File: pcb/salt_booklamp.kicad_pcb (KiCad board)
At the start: 2 copper layers, 45.1 x 45.1 mm, 24 parts, among them J1 USB-C31-S-RA-CS1E-BK-T/R, P1 PIC-TC2050-IDC, U1 PIC16F15213-I/SN, U2 BQ21040DBVR, U3 TPS61158DRVR

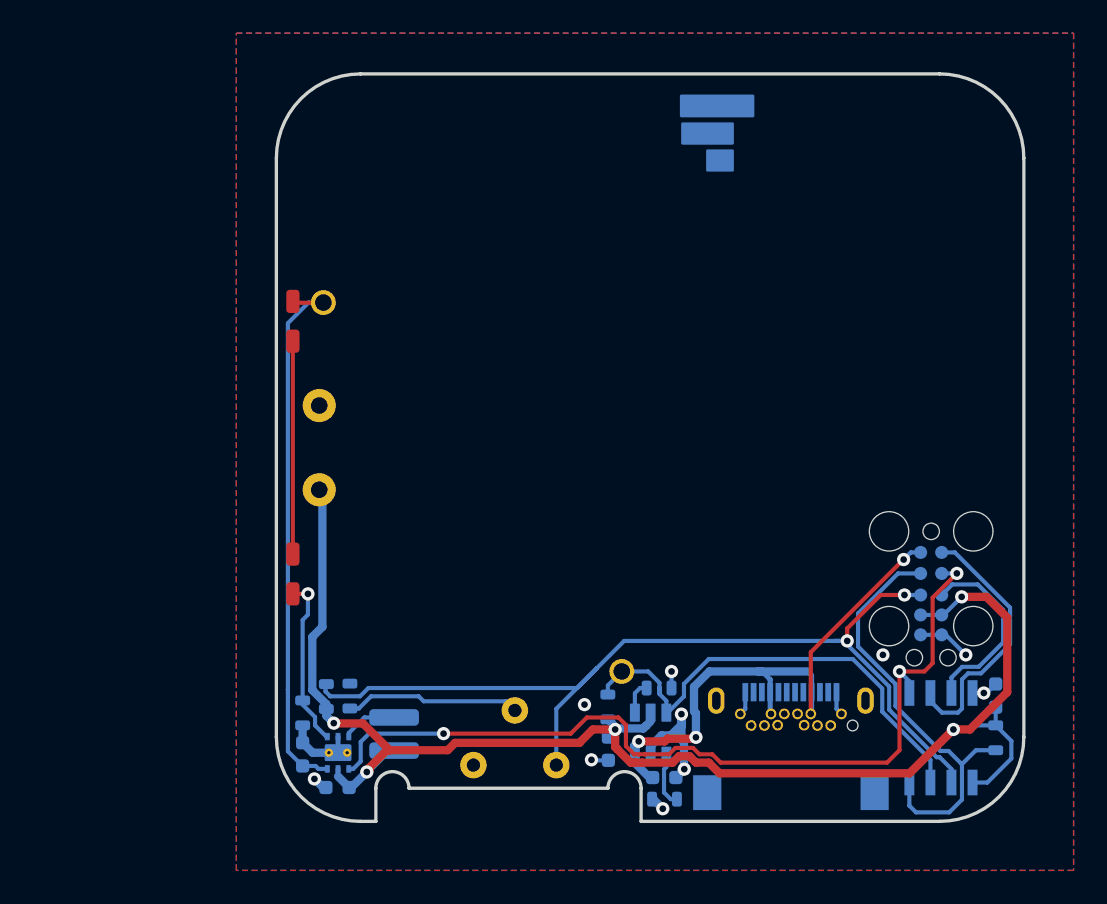
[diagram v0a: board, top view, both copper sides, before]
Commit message: Changed 0603 parts to 0402, assigned 0402 uF cap MPN, still need to assign 0402 Resistor MPNs
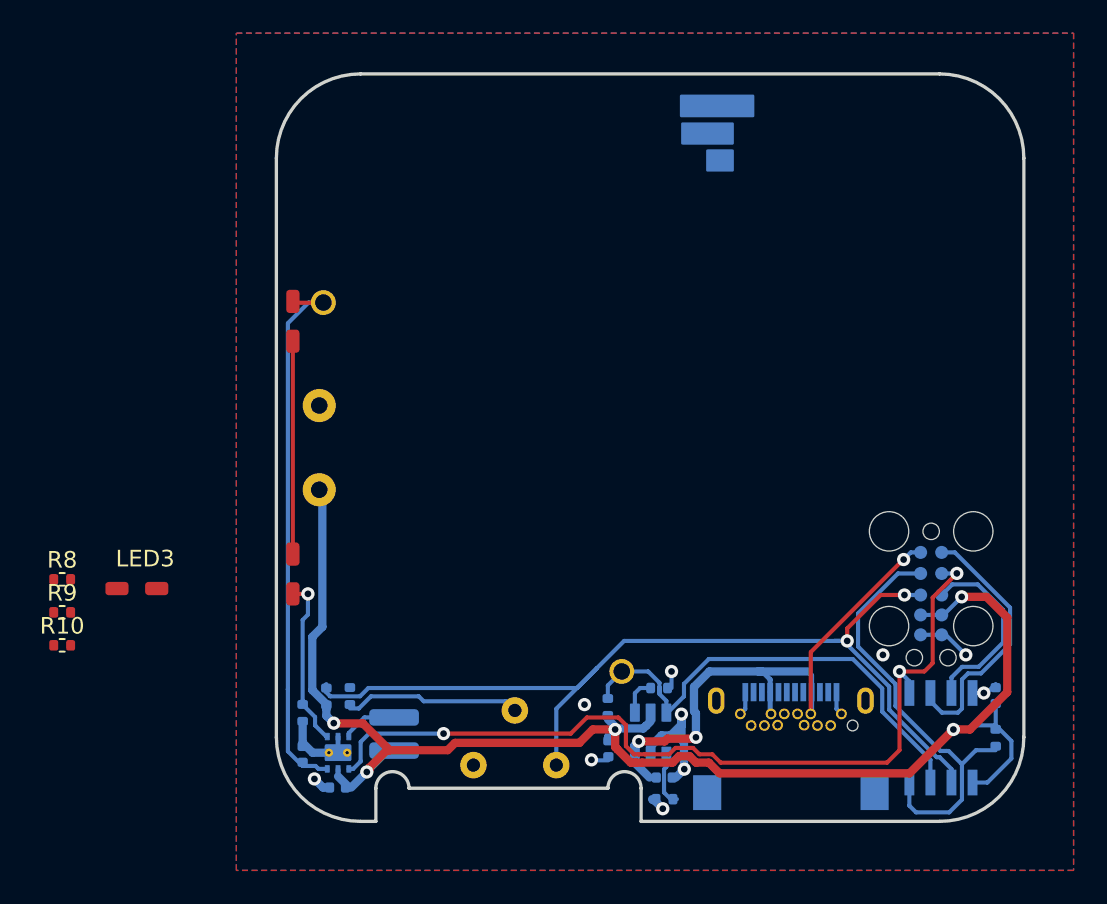
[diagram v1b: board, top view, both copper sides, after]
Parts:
- added LED3: SMS1105UWDW, salt_booklamp_footprints:LED_SMS1105UWDW, F.Cu at (193.3, 137.5)
- added R10: 5k1, Resistor_SMD:R_0402_1005Metric, F.Cu at (188.8, 141.0)
- added R8: 0r0, Resistor_SMD:R_0402_1005Metric, F.Cu at (188.8, 137.0)
- added R9: 5k1, Resistor_SMD:R_0402_1005Metric, F.Cu at (188.8, 139.0)
- C1, C2, C3, C4, C5: footprint salt_booklamp_footprints:cap_0603 -> Capacitor_SMD:C_0402_1005Metric
- R1, R2, R3, R4, R5, R6, R7: footprint salt_booklamp_footprints:res_0603 -> Resistor_SMD:R_0402_1005Metric
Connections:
- J1 pad A5: unconnected-(J1-CC1-PadA5) -> Net-(J1-CC1)
- J1 pad B5: unconnected-(J1-CC2-PadB5) -> Net-(J1-CC2)
- LED2 pad A: Net-(LED1-k) -> Net-(LED2-a)

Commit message: Changed MCU to smaller DFN package, add Connector footprint to PCB (very big), add shield pins to USB footprint to remove warning
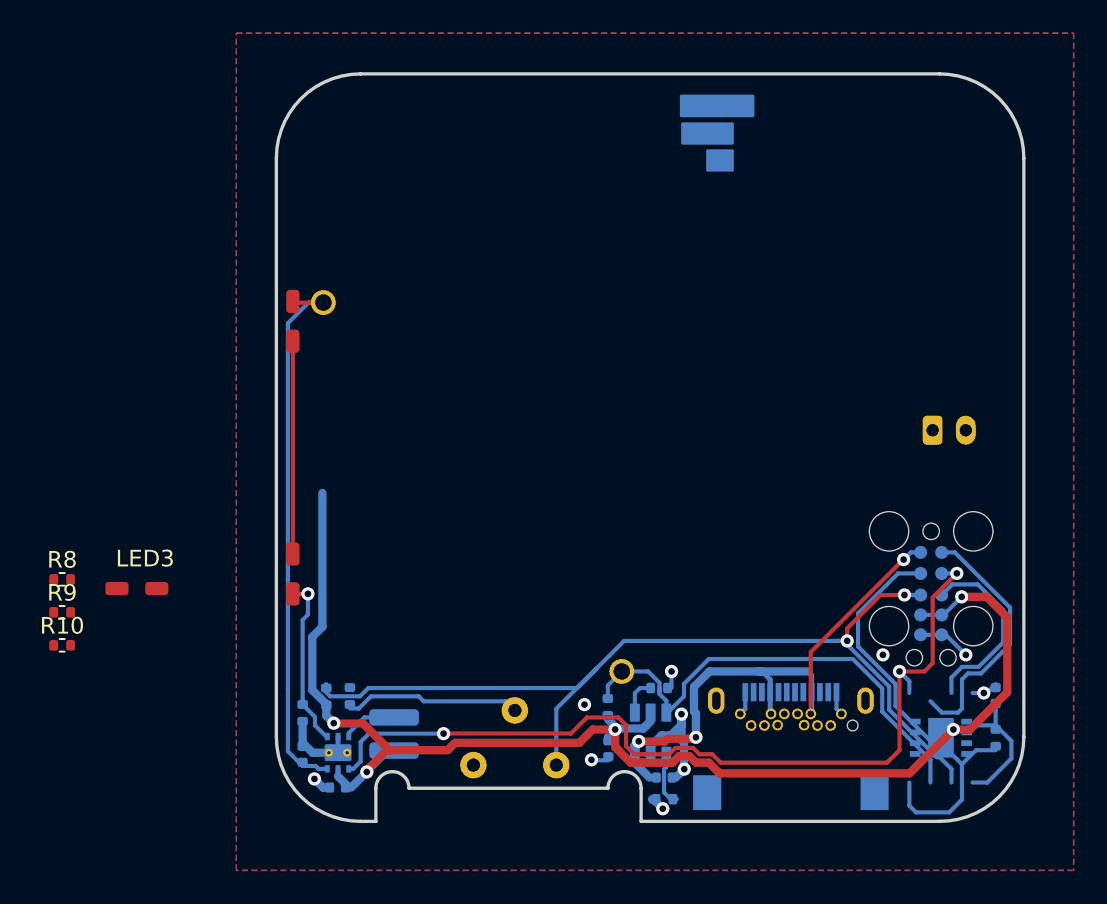
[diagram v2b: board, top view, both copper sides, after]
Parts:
- BATT1: value 1578 -> S2B-PH-K-S; footprint salt_booklamp_footprints:PRT-13851 -> GymTimer:JST_PH_S2B-PH-K_1x02_P2.00mm_Horizontal
- U1: footprint salt_booklamp_footprints:SOIC-8 - PIC16F15213 -> GymTimer:DFN-8-1EP_3x3mm_P0.65mm_EP1.55x2.4mm
- moved BATT1 37.0 mm to (241.3, 128.0), turned to 0 degrees
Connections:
- BATT1 pad 1: +3.7_VBATT -> GND
- BATT1 pad 2: GND -> +3.7_VBATT
- J1 pad 0: (no net) -> GND

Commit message: Start placement - new LED placement
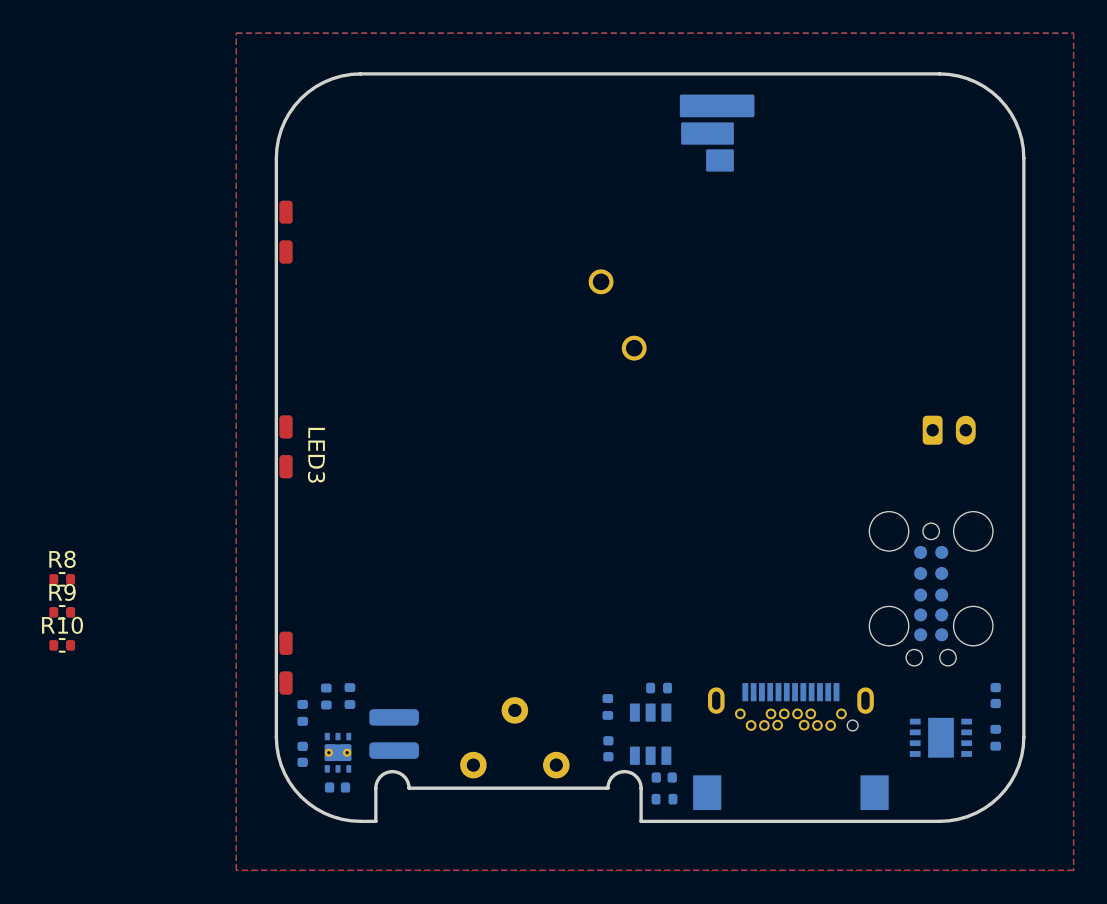
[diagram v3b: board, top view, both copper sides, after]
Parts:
- moved ~{TP_CHG}1 19.5 mm to (223.3, 123.0)
- moved TP_LED_DRV1 16.8 mm to (221.3, 119.0)
- moved LED3 12.4 mm to (202.3, 129.0), turned to -90 degrees
- moved LED2 5.40 mm to (202.3, 142.0)
- moved LED1 5.40 mm to (202.3, 116.0)
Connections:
- R5 pad 1: Net-(P1-~{MCLR}) -> Net-(P1-ICSPDAT)
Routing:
- net +3.7_VBATT: track 91.4 -> 0.00 mm, vias 5 -> 0
- net /~{SWITCH}: track 58.2 -> 0.00 mm, vias 2 -> 0
- net /LED_CTRL: track 53.1 -> 0.00 mm, vias 3 -> 0
- net +5V_USB: track 34.9 -> 0.00 mm, vias 3 -> 0
- net /LED_DRV: track 33.1 -> 0.00 mm
- net /~{CHARGING}: track 29.2 -> 0.00 mm
- net Net-(P1-~{MCLR}): track 26.3 -> 0.00 mm
- net GND: track 22.8 -> 0.00 mm, vias 10 -> 0
- net Net-(P1-ICSPCLK): track 15.5 -> 0.00 mm
- net Net-(LED1-k): track 12.8 -> 0.00 mm
- net Net-(P1-ICSPDAT): track 11.5 -> 0.00 mm
- net Net-(R7-Pad2): track 10.6 -> 0.00 mm
- net Net-(LED2-k): track 10.3 -> 0.00 mm, vias 1 -> 0
- net Net-(U3-LX): track 3.33 -> 0.00 mm
- net Net-(U2-ISET): track 3.22 -> 0.00 mm
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
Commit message: Placement work
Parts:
- R10, R8, R9: moved to B.Cu
- moved R10 10.5 mm to (196.0, 148.5), turned to 180 degrees
- moved R8 10.5 mm to (196.0, 144.6), turned to 180 degrees
- moved R9 10.5 mm to (196.0, 146.5), turned to 180 degrees
- moved R7 2.05 mm to (205.8, 146.0)
- moved R3 1.99 mm to (204.7, 146.0)
- moved R2 1.77 mm to (203.5, 146.8)
- moved C4 1.27 mm to (203.5, 148.8)
- moved U3 0.99 mm to (205.4, 148.4)
- moved C5 0.75 mm to (205.4, 150.3)

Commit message: Placement work
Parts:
- moved R8 2.79 mm to (198.8, 145.0)
- moved R10 2.79 mm to (198.8, 149.0)
- moved R9 2.79 mm to (198.8, 147.0)
- moved R4 0.37 mm to (221.8, 145.0)
- moved R6 0.22 mm to (225.0, 150.0)
- moved C1 0.06 mm to (225.0, 148.9)
- moved C2 0.06 mm to (221.8, 147.2)
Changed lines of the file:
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@@
 			(psa4output no)
 			(plot_black_and_white yes)
-			(plotinvisibletext no)
 			(sketchpadsonfab no)
 			(plotpadnumbers no)
@@
 	(footprint "Capacitor_SMD:C_0402_1005Metric"
 		(layer "B.Cu")
-		(at 225.093116 148.932371)
+		(at 225.032 148.932371)
 		(descr "Capacitor SMD 0402 (1005 Metric), square (rectangular) end terminal, IPC_7351 nominal, (Body size source: IPC-SM-782 page 76, https://www.pcb-3d.com/wordpress/wp-content/uploads/ipc-sm-782a_amendment_1_and_2.pdf), generated with kicad-footprint-generator")
 		(tags "capacitor")
@@
 	(footprint "Resistor_SMD:R_0402_1005Metric"
 		(layer "B.Cu")
-		(at 196.032 148.532 180)
+		(at 198.782 149.012 180)
 		(descr "Resistor SMD 0402 (1005 Metric), square (rectangular) end terminal, IPC_7351 nominal, (Body size source: IPC-SM-782 page 72, https://www.pcb-3d.com/wordpress/wp-content/uploads/ipc-sm-782a_amendment_1_and_2.pdf), generated with kicad-footprint-generator")
 		(tags "resistor")
@@
 	(footprint "Capacitor_SMD:C_0402_1005Metric"
 		(layer "B.Cu")
-		(at 221.721579 147.194047 -90)
+		(at 221.782 147.194047 -90)
 		(descr "Capacitor SMD 0402 (1005 Metric), square (rectangular) end terminal, IPC_7351 nominal, (Body size source: IPC-SM-782 page 76, https://www.pcb-3d.com/wordpress/wp-content/uploads/ipc-sm-782a_amendment_1_and_2.pdf), generated with kicad-footprint-generator")
 		(tags "capacitor")
@@
 	(footprint "Resistor_SMD:R_0402_1005Metric"
 		(layer "B.Cu")
-		(at 225.107866 150.236383 180)
+		(at 225.032 150.032 180)
 		(descr "Resistor SMD 0402 (1005 Metric), square (rectangular) end terminal, IPC_7351 nominal, (Body size source: IPC-SM-782 page 72, https://www.pcb-3d.com/wordpress/wp-content/uploads/ipc-sm-782a_amendment_1_and_2.pdf), generated with kicad-footprint-generator")
 		(tags "resistor")
@@
 	(footprint "Resistor_SMD:R_0402_1005Metric"
 		(layer "B.Cu")
-		(at 196.032 146.542 180)
+		(at 198.782 147.022 180)
 		(descr "Resistor SMD 0402 (1005 Metric), square (rectangular) end terminal, IPC_7351 nominal, (Body size source: IPC-SM-782 page 72, https://www.pcb-3d.com/wordpress/wp-content/uploads/ipc-sm-782a_amendment_1_and_2.pdf), generated with kicad-footprint-generator")
 		(tags "resistor")
@@
 	(footprint "Resistor_SMD:R_0402_1005Metric"
 		(layer "B.Cu")
-		(at 221.689761 144.674153 -90)
+		(at 221.782 145.032 -90)
 		(descr "Resistor SMD 0402 (1005 Metric), square (rectangular) end terminal, IPC_7351 nominal, (Body size source: IPC-SM-782 page 72, https://www.pcb-3d.com/wordpress/wp-content/uploads/ipc-sm-782a_amendment_1_and_2.pdf), generated with kicad-footprint-generator")
 		(tags "resistor")
@@
 	(footprint "Resistor_SMD:R_0402_1005Metric"
 		(layer "B.Cu")
-		(at 196.032 144.552 180)
+		(at 198.782 145.032 180)
 		(descr "Resistor SMD 0402 (1005 Metric), square (rectangular) end terminal, IPC_7351 nominal, (Body size source: IPC-SM-782 page 72, https://www.pcb-3d.com/wordpress/wp-content/uploads/ipc-sm-782a_amendment_1_and_2.pdf), generated with kicad-footprint-generator")
 		(tags "resistor")

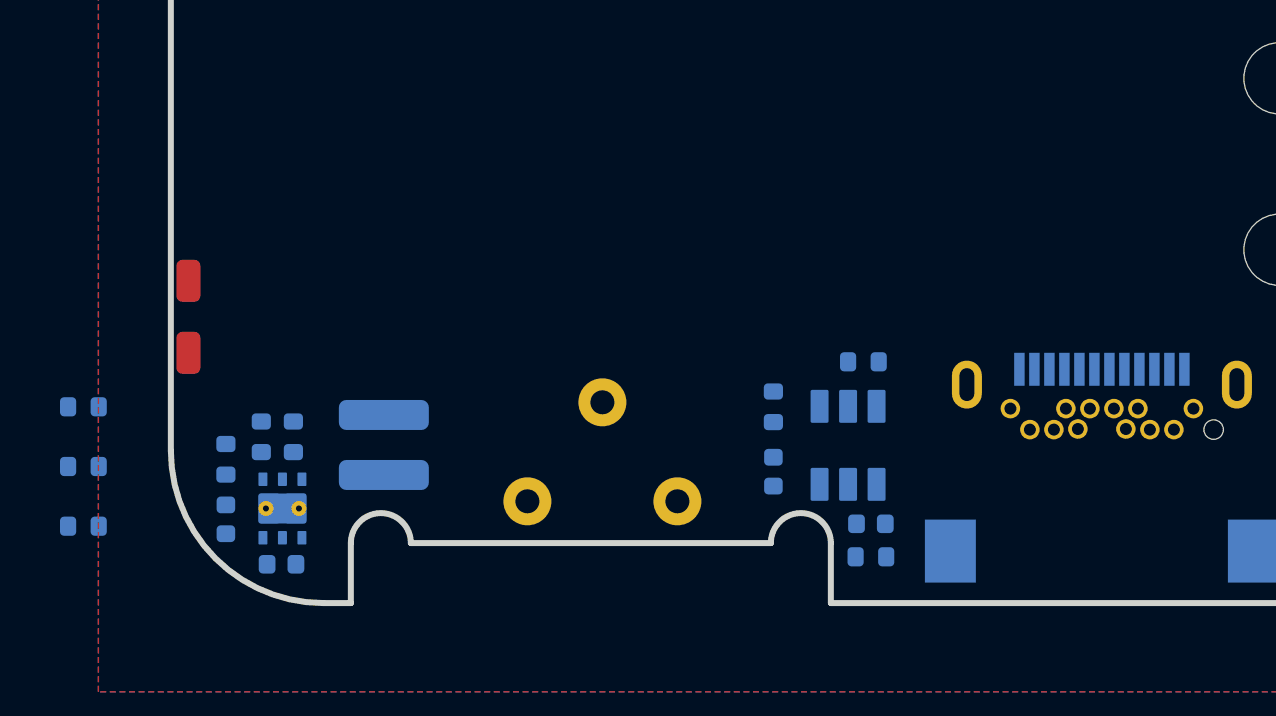
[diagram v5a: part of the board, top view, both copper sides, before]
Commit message: changed placement of a couple resistors to achieve daily commit
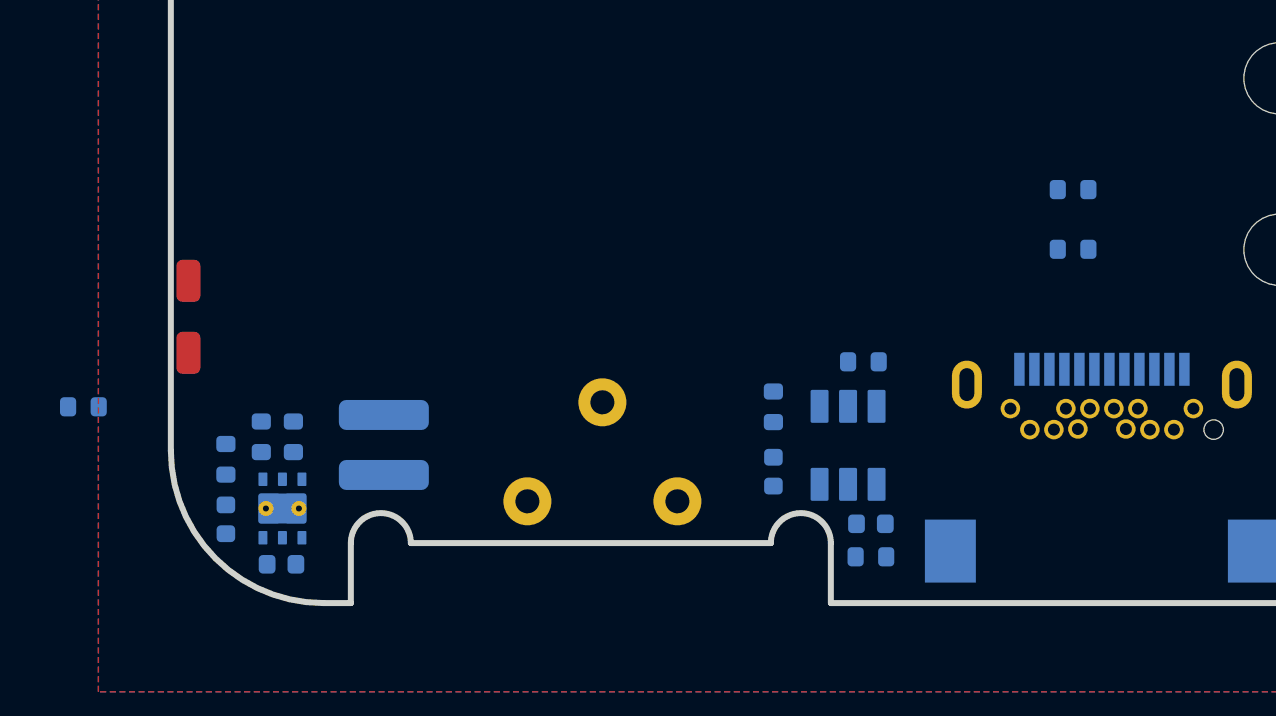
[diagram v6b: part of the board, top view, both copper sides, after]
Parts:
- moved R10 34.3 mm to (231.8, 139.8)
- moved R9 34.3 mm to (231.8, 137.8)
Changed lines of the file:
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@@
 	(footprint "Resistor_SMD:R_0402_1005Metric"
 		(layer "B.Cu")
-		(at 198.782 149.012 180)
+		(at 231.772 139.782 180)
 		(descr "Resistor SMD 0402 (1005 Metric), square (rectangular) end terminal, IPC_7351 nominal, (Body size source: IPC-SM-782 page 72, https://www.pcb-3d.com/wordpress/wp-content/uploads/ipc-sm-782a_amendment_1_and_2.pdf), generated with kicad-footprint-generator")
 		(tags "resistor")
@@
 	(footprint "Resistor_SMD:R_0402_1005Metric"
 		(layer "B.Cu")
-		(at 198.782 147.022 180)
+		(at 231.772 137.792 180)
 		(descr "Resistor SMD 0402 (1005 Metric), square (rectangular) end terminal, IPC_7351 nominal, (Body size source: IPC-SM-782 page 72, https://www.pcb-3d.com/wordpress/wp-content/uploads/ipc-sm-782a_amendment_1_and_2.pdf), generated with kicad-footprint-generator")
 		(tags "resistor")
